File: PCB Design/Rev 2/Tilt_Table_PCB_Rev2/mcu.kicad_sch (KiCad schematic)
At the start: 22 parts, among them J10 X_SERVO_HDR, J11 GPIO_HDR, J5 BOOT_HDR, J6 USB_B_Micro, J7 SWD, J8 Touch_Panel_HDR, J9 Y_SERVO_HDR, U3 TLV75533PDBV, U4 STM32F042F6Px

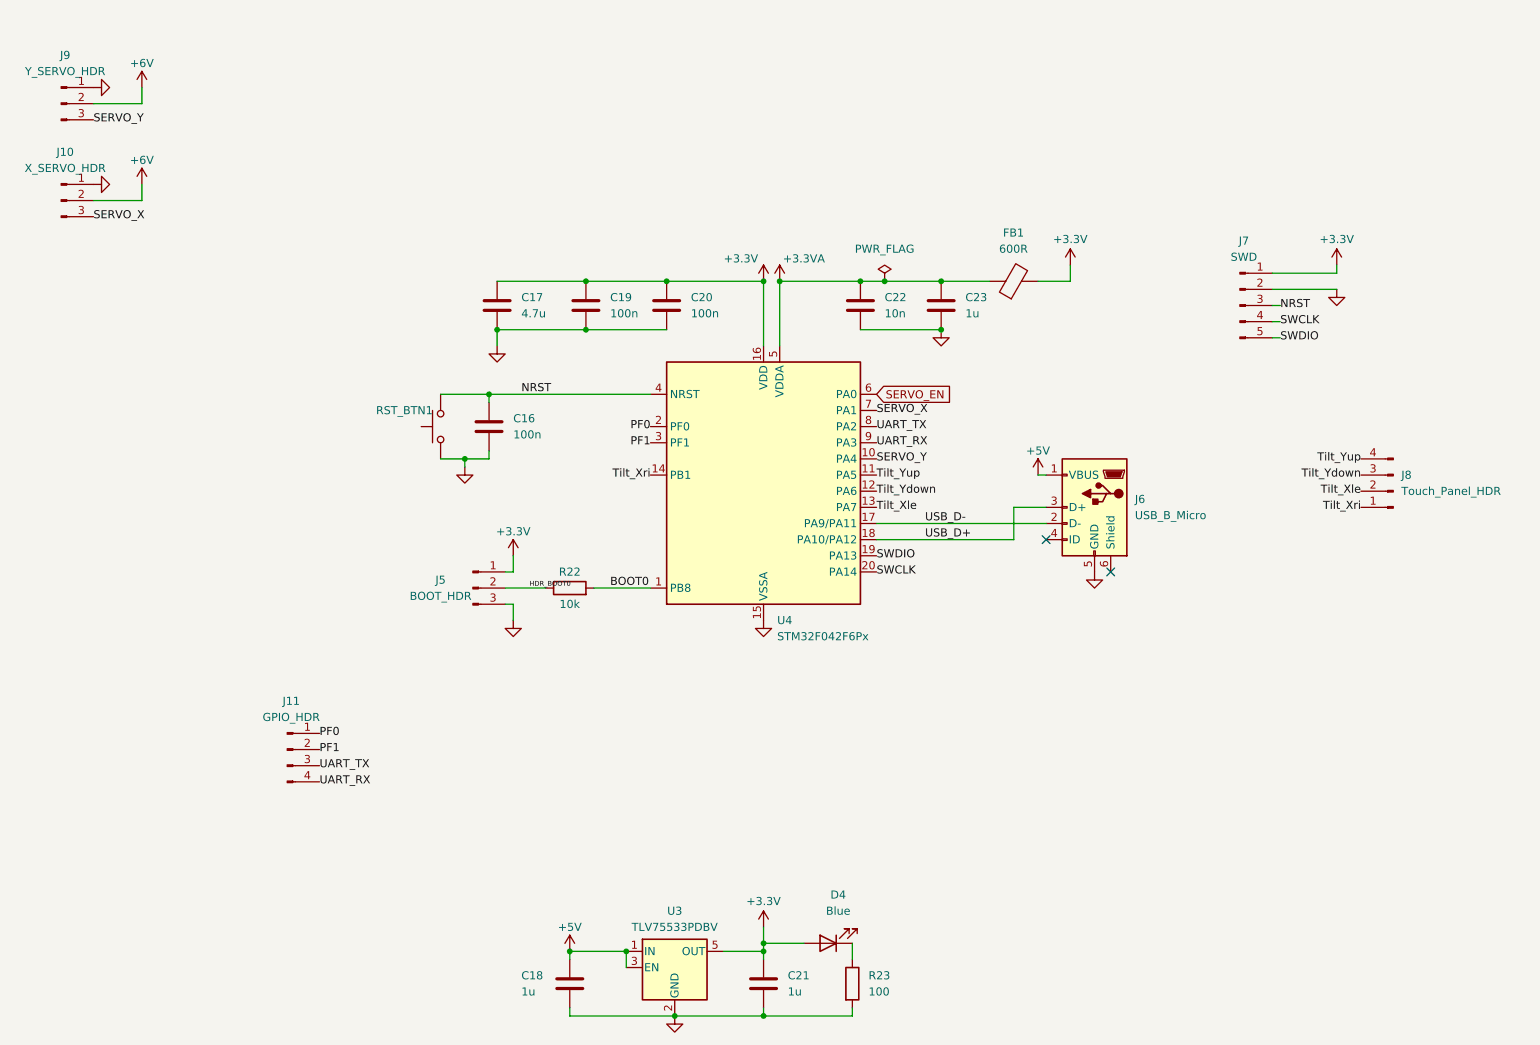
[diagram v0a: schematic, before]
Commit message: Rev 2 schematic updated
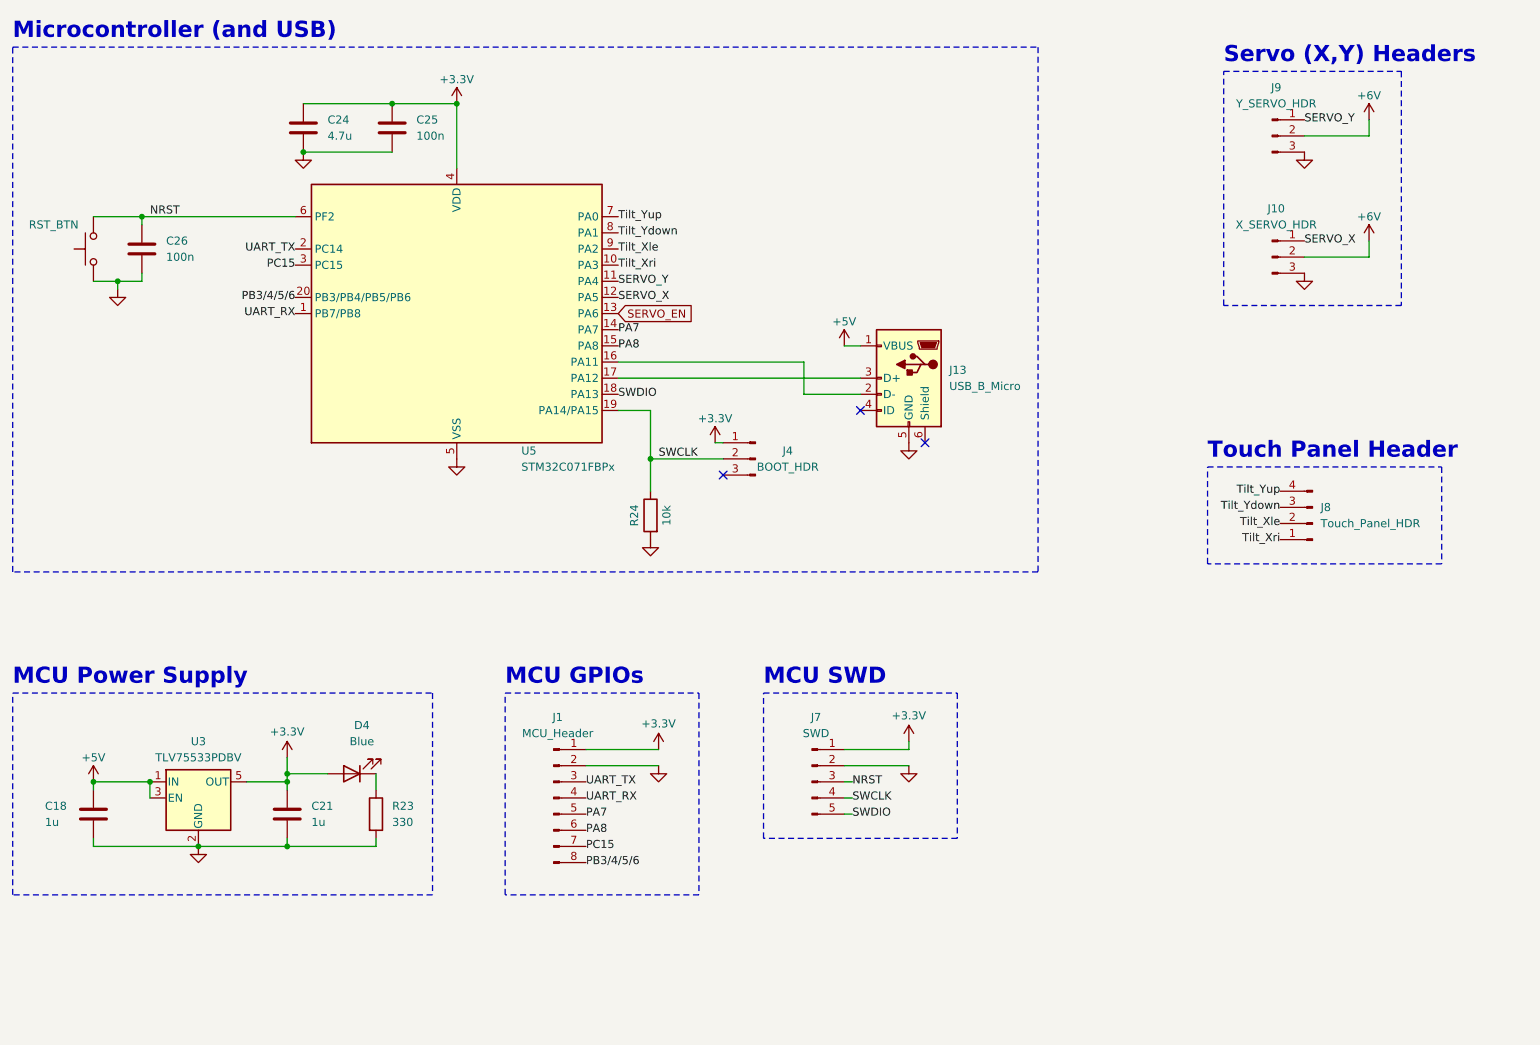
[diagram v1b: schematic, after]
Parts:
- removed C16, C19, C20: 100n, Capacitor_SMD:C_0603_1608Metric, symbol Device:C
- removed C17: 4.7u, Capacitor_SMD:C_0805_2012Metric, symbol Device:C
- removed C22: 10n, Capacitor_SMD:C_0603_1608Metric, symbol Device:C
- removed C23: 1u, Capacitor_SMD:C_0603_1608Metric, symbol Device:C
- removed FB1: 600R, Inductor_SMD:L_0603_1608Metric, symbol Device:FerriteBead
- removed J11: GPIO_HDR, Connector_PinHeader_2.54mm:PinHeader_1x04_P2.54mm_Vertical, symbol Connector:Conn_01x04_Pin
- removed J5: BOOT_HDR, Connector_PinHeader_2.54mm:PinHeader_1x03_P2.54mm_Vertical, symbol Connector:Conn_01x03_Pin
- removed J6: USB_B_Micro, Connector_USB:USB_Micro-B_Amphenol_10118194-0001LF_Horizontal, symbol Connector:USB_B_Micro
- removed R22: 10k, Resistor_SMD:R_0603_1608Metric, symbol Device:R
- removed RST_BTN1: RST_SW, Button_Switch_SMD:SW_SPST_PTS645Sx43SMTR92, symbol Switch:SW_Push
- removed U4: STM32F042F6Px, Package_SO:TSSOP-20_4.4x6.5mm_P0.65mm, symbol MCU_ST_STM32F0:STM32F042F6Px
- added C24: 4.7u, Capacitor_SMD:C_0805_2012Metric, symbol Device:C
- added C25, C26: 100n, Capacitor_SMD:C_0603_1608Metric, symbol Device:C
- added J1: MCU_Header, symbol Connector:Conn_01x08_Pin
- added J13: USB_B_Micro, Connector_USB:USB_Micro-B_Amphenol_10118194-0001LF_Horizontal, symbol Connector:USB_B_Micro
- added J4: BOOT_HDR, Connector_PinHeader_2.54mm:PinHeader_1x03_P2.54mm_Vertical, symbol Connector:Conn_01x03_Pin
- added R24: 10k, Resistor_SMD:R_0603_1608Metric, symbol Device:R
- added RST_BTN: RST_SW, Button_Switch_SMD:SW_SPST_PTS645Sx43SMTR92, symbol Switch:SW_Push
- added U5: STM32C071FBPx, Package_SO:TSSOP-20_4.4x6.5mm_P0.65mm, symbol MCU_ST_STM32C0:STM32C071FBPx
- R23: value 100 -> 330
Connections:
- net +3.3V: now also C24.1, C25.1, J1.1 (Pin_1), J4.1 (Pin_1), U5.4 (VDD)
- net +5V: now also J13.1 (VBUS)
- net GND: now also J10.3 (Pin_3), J9.3 (Pin_3), C24.2, C25.2, C26.2, J1.2 (Pin_2), J13.5 (GND), R24.2, RST_BTN.1, U5.5 (VSS); no longer J10.1 (Pin_1), J9.1 (Pin_1)
- net NRST: now also C26.1, RST_BTN.2, U5.6 (PF2)
- net SERVO_EN: now also U5.13 (PA6)
- net SERVO_X: now also J10.1 (Pin_1), U5.12 (PA5); no longer J10.3 (Pin_3)
- net SERVO_Y: now also J9.1 (Pin_1), U5.11 (PA4); no longer J9.3 (Pin_3)
- net SWCLK: now also J4.2 (Pin_2), R24.1, U5.19 (PA14/PA15)
- net SWDIO: now also U5.18 (PA13)
- net Tilt_Xle: now also U5.9 (PA2)
- net Tilt_Xri: now also U5.10 (PA3)
- net Tilt_Ydown: now also U5.8 (PA1)
- net Tilt_Yup: now also U5.7 (PA0)
- net UART_RX: now also J1.4 (Pin_4), U5.1 (PB7/PB8)
- net UART_TX: now also J1.3 (Pin_3), U5.2 (PC14)
- new net: J13.2 (D-), U5.16 (PA11)
- new net: J13.3 (D+), U5.17 (PA12)
- new net PA7: J1.5 (Pin_5), U5.14 (PA7)
- new net PA8: J1.6 (Pin_6), U5.15 (PA8)
- new net PB3/4/5/6: J1.8 (Pin_8), U5.20 (PB3/PB4/PB5/PB6)
- new net PC15: J1.7 (Pin_7), U5.3 (PC15)
- no-connect marks 2 -> 3
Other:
- note added: "MCU GPIOs"
- note added: "MCU Power Supply"
- note added: "MCU SWD"
- note added: "Microcontroller (and USB)"
- note added: "Servo (X,Y) Headers"
- note added: "Touch Panel Header"
- moved on the sheet: C18, C21, D4, J10, J7, J8, J9, R23, U3

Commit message: PCB Rev 2 Update
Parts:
- removed RST_BTN: RST_SW, Button_Switch_SMD:SW_SPST_PTS645Sx43SMTR92, symbol Switch:SW_Push
- added SW1: RST_BTN, Button_Switch_SMD:SW_SPST_PTS645Sx43SMTR92, symbol Switch:SW_Push
- J5: renamed from J1; footprint (none) -> Connector_PinHeader_2.54mm:PinHeader_1x08_P2.54mm_Vertical
- renumbered C18 to C16, C26 to C17, C21 to C18, C24 to C19, C25 to C20, J8 to J11, J4 to J6, J13 to J8, R23 to R22, R24 to R23, U5 to U4
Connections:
- net GND: now also SW1.1
- net NRST: now also SW1.2
- net PA8: now also J5.4 (Pin_4); no longer J5.6 (Pin_6)
- net PB3/4/5/6: now also J5.3 (Pin_3); no longer J5.8 (Pin_8)
- net PC15: now also J5.6 (Pin_6); no longer J5.7 (Pin_7)
- net UART_RX: now also J5.8 (Pin_8); no longer J5.4 (Pin_4)
- net UART_TX: now also J5.7 (Pin_7); no longer J5.3 (Pin_3)
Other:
- company: (none) -> Made by Jasper Tan
- title: (none) -> Tilt Plate Board

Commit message: PCB Rev 2 Update
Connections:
- net PA7: now also J5.3 (Pin_3); no longer J5.5 (Pin_5)
- net PB3/4/5/6: now also J5.5 (Pin_5); no longer J5.3 (Pin_3)
- net USB_D-: now reaches J8.2 (D-), U4.16 (PA11)
- net USB_D+: now reaches J8.3 (D+), U4.17 (PA12)

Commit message: PCB Rev 2 Layout Complete - Prior to PCB Order
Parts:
- removed J7: SWD, Connector_PinHeader_2.54mm:PinHeader_1x05_P2.54mm_Vertical, symbol Connector:Conn_01x05_Pin
- added J12: SWD, Connector_PinHeader_2.54mm:PinHeader_1x03_P2.54mm_Vertical, symbol Connector:Conn_01x03_Pin
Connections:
- net NRST: now also J12.1 (Pin_1)
- net PA7: now also J5.5 (Pin_5); no longer J5.3 (Pin_3)
- net PB3/4/5/6: now also J5.3 (Pin_3); no longer J5.5 (Pin_5)
- net SWCLK: now also J12.2 (Pin_2)
- net SWDIO: now also J12.3 (Pin_3)
- net UART_RX: now also J5.7 (Pin_7); no longer J5.8 (Pin_8)
- net UART_TX: now also J5.8 (Pin_8); no longer J5.7 (Pin_7)
